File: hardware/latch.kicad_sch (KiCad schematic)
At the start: 4 parts, among them K2 2-1393779-0 TE, Q4 BSS123

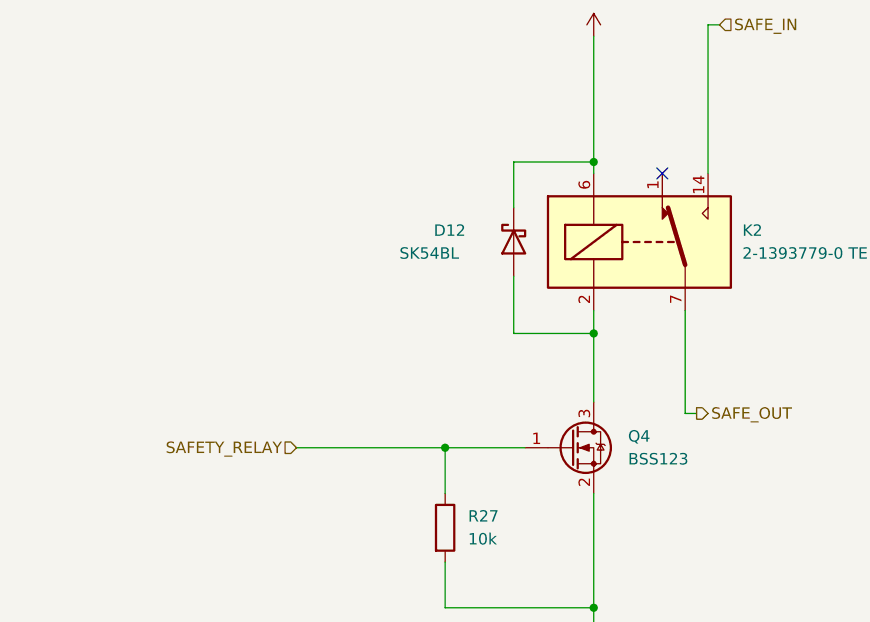
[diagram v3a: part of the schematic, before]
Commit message: 0xERC State
Schematic needs only simulation and veryfying component choice for now
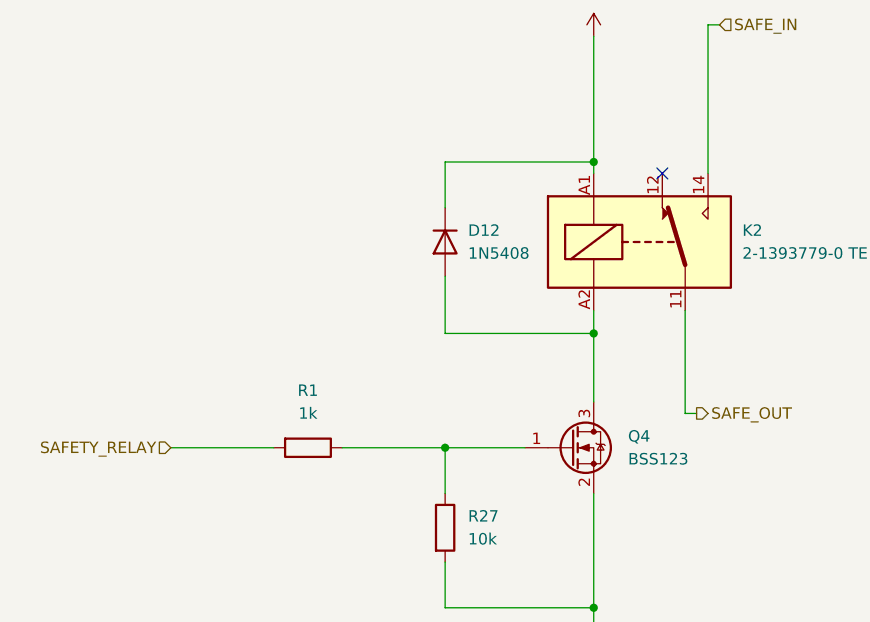
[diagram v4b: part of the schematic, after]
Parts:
- removed D12: SK54BL, Diode_SMD:D_SMB, symbol Device:D_Schottky
- added D12: 1N5408, Diode_THT:D_DO-201AD_P15.24mm_Horizontal, symbol Diode:1N5408
- added R1: 1k, Resistor_SMD:R_0603_1608Metric, symbol Device:R
- K2: footprint Relay_THT:Relay_StandexMeder_DIP_LowProfile -> PUTM_Kicad_FOOTPRINTS:TE Relay; symbol Relay:DIPxx-1Cxx-51x -> PUTM_SYMBOLS:EBS_safety_realy
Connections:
- net +24V: now also K2.A1, D12.1 (K); no longer K2.6
- net SAFETY_RELAY: now also R1.2; no longer Q4.1 (G), R27.1
- net SAFE_OUT: now also K2.11; no longer K2.7, K2.8
- net at Q4.3 (D): now also K2.A2, D12.2 (A); no longer K2.2
- new net: Q4.1 (G), R1.1, R27.1
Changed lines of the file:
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@@
     (company "PUT Motorsport")
   )
+  (junction (at 127 107.95) (diameter 0) (color 0 0 0 0)
+  )
   (junction (at 143.51 125.73) (diameter 0) (color 0 0 0 0)
-  )
-  (junction (at 127 107.95) (diameter 0) (color 0 0 0 0)
   )
   (junction (at 143.51 76.2) (diameter 0) (color 0 0 0 0)
@@
   )
   (no_connect (at 151.13 77.47))
-  (wire (pts (xy 110.49 107.95) (xy 127 107.95))
-    (stroke (width 0) (type default) (color 0 0 0 0))
-  )
-  (wire (pts (xy 134.62 88.9) (xy 134.62 95.25))
-    (stroke (width 0) (type default) (color 0 0 0 0))
-  )
   (wire (pts (xy 143.51 125.73) (xy 143.51 134.62))
     (stroke (width 0) (type default) (color 0 0 0 0))
@@
     (stroke (width 0) (type default) (color 0 0 0 0))
   )
-  (wire (pts (xy 134.62 95.25) (xy 143.51 95.25))
+  (wire (pts (xy 127 95.25) (xy 143.51 95.25))
     (stroke (width 0) (type default) (color 0 0 0 0))
   )
@@
     (stroke (width 0) (type default) (color 0 0 0 0))
   )
-  (wire (pts (xy 134.62 81.28) (xy 134.62 76.2))
+  (wire (pts (xy 127 81.28) (xy 127 76.2))
+    (stroke (width 0) (type default) (color 0 0 0 0))
+  )
+  (wire (pts (xy 127 76.2) (xy 143.51 76.2))
+    (stroke (width 0) (type default) (color 0 0 0 0))
+  )
+  (wire (pts (xy 96.52 107.95) (xy 107.95 107.95))
+    (stroke (width 0) (type default) (color 0 0 0 0))
+  )
+  (wire (pts (xy 115.57 107.95) (xy 127 107.95))
     (stroke (width 0) (type default) (color 0 0 0 0))
   )
@@
     (stroke (width 0) (type default) (color 0 0 0 0))
   )
-  (wire (pts (xy 134.62 76.2) (xy 143.51 76.2))
-    (stroke (width 0) (type default) (color 0 0 0 0))
-  )
   (wire (pts (xy 156.21 60.96) (xy 157.48 60.96))
     (stroke (width 0) (type default) (color 0 0 0 0))
   )
   (wire (pts (xy 143.51 113.03) (xy 143.51 125.73))
+    (stroke (width 0) (type default) (color 0 0 0 0))
+  )
+  (wire (pts (xy 127 95.25) (xy 127 88.9))
     (stroke (width 0) (type default) (color 0 0 0 0))
   )
@@
     (effects (font (size 1.27 1.27)) (justify left))
   )
-  (hierarchical_label "SAFETY_RELAY" (shape input) (at 110.49 107.95 180)
+  (hierarchical_label "SAFETY_RELAY" (shape input) (at 96.52 107.95 180)
     (effects (font (size 1.27 1.27)) (justify right))
   )
-  (symbol (lib_id "Relay:DIPxx-1Cxx-51x") (at 148.59 85.09 0) (unit 1)
+  (symbol (lib_id "Diode:1N5408") (at 127 85.09 90) (mirror x) (unit 1)
+    (in_bom yes) (on_board yes) (fields_autoplaced)
+    (property "Reference" "D12" (id 0) (at 129.54 83.8199 90)
+      (effects (font (size 1.27 1.27)) (justify right))
+    )
+    (property "Value" "1N5408" (id 1) (at 129.54 86.3599 90)
+      (effects (font (size 1.27 1.27)) (justify right))
+    )
+    (property "Footprint" "Diode_THT:D_DO-201AD_P15.24mm_Horizontal" (id 2) (at 131.445 85.09 0)
+      (effects (font (size 1.27 1.27)) hide)
+    )
+    (property "Datasheet" "http://www.vishay.com/docs/88516/1n5400.pdf" (id 3) (at 127 85.09 0)
+      (effects (font (size 1.27 1.27)) hide)
+    )
+    (pin "1")
+    (pin "2")
+  )
+  (symbol (lib_id "PUTM_SYMBOLS:EBS_safety_realy") (at 148.59 85.09 0) (unit 1)
     (in_bom yes) (on_board yes) (fields_autoplaced)
     (property "Reference" "K2" (id 0) (at 160.02 83.8199 0)
@@
       (effects (font (size 1.27 1.27)) (justify left))
     )
-    (property "Footprint" "Relay_THT:Relay_StandexMeder_DIP_LowProfile" (id 2) (at 160.02 86.36 0)
-      (effects (font (size 1.27 1.27)) (justify left) hide)
-    )
-    (property "Datasheet" "https://standexelectronics.com/wp-content/uploads/datasheet_reed_relay_DIP.pdf" (id 3) (at 148.59 85.09 0)
+    (property "Footprint" "PUTM_Kicad_FOOTPRINTS:TE Relay" (id 2) (at 148.59 76.2 0)
       (effects (font (size 1.27 1.27)) hide)
     )
-    (pin "1")
+    (property "Datasheet" "https://standexelectronics.com/wp-content/uploads/datasheet_reed_relay_DIP.pdf" (id 3) (at 148.59 76.2 0)
+      (effects (font (size 1.27 1.27)) hide)
+    )
+    (pin "11")
+    (pin "12")
     (pin "14")
-    (pin "2")
-    (pin "6")
-    (pin "7")
-    (pin "8")
+    (pin "A1")
+    (pin "A2")
   )
   (symbol (lib_id "power:GND") (at 143.51 134.62 0) (unit 1)
@@
     (pin "3")
   )
-  (symbol (lib_id "Device:D_Schottky") (at 134.62 85.09 90) (mirror x) (unit 1)
-    (in_bom yes) (on_board yes)
-    (property "Reference" "D12" (id 0) (at 125.73 83.82 90)
-      (effects (font (size 1.27 1.27)) (justify right))
-    )
-    (property "Value" "SK54BL" (id 1) (at 121.92 86.36 90)
-      (effects (font (size 1.27 1.27)) (justify right))
-    )
-    (property "Footprint" "Diode_SMD:D_SMB" (id 2) (at 134.62 85.09 0)
-      (effects (font (size 1.27 1.27)) hide)
-    )
-    (property "Datasheet" "~" (id 3) (at 134.62 85.09 0)
-      (effects (font (size 1.27 1.27)) hide)
-    )
-    (pin "1")
-    (pin "2")
-  )
   (symbol (lib_id "power:+24V") (at 143.51 62.23 0) (unit 1)
     (in_bom yes) (on_board yes) (fields_autoplaced)
@@
       (effects (font (size 1.27 1.27)) hide)
     )
+    (pin "1")
+    (pin "2")
+  )
+  (symbol (lib_id "Device:R") (at 111.76 107.95 270) (unit 1)
+    (in_bom yes) (on_board yes) (fields_autoplaced)
+    (property "Reference" "R1" (id 0) (at 111.76 101.6 90))
+    (property "Value" "1k" (id 1) (at 111.76 104.14 90))
+    (property "Footprint" "Resistor_SMD:R_0603_1608Metric" (id 2) (at 111.76 106.172 90)
+      (effects (font (size 1.27 1.27)) hide)
+    )
+    (property "Datasheet" "~" (id 3) (at 111.76 107.95 0)
+      (effects (font (size 1.27 1.27)) hide)
+    )

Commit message: working simulations, assigned footprints
"nightly" relase
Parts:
- removed K2: 2-1393779-0 TE, PUTM_Kicad_FOOTPRINTS:TE Relay, symbol PUTM_SYMBOLS:EBS_safety_realy
- added K2: FINDER-30.22, Relay_THT:Relay_DPDT_Finder_30.22, symbol Relay:FINDER-30.22
- D12: value 1N5408 -> SK36A; footprint Diode_THT:D_DO-201AD_P15.24mm_Horizontal -> Diode_SMD:D_SMA_Handsoldering
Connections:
- net +24V: now also K2.A1
- net SAFE_IN: now also K2.14
- net SAFE_OUT: now also K2.11
- net at D12.2 (A), Q4.3 (D): now also K2.A2
- no-connect marks 1 -> 4
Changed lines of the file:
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@@
   (junction (at 143.51 95.25) (diameter 0) (color 0 0 0 0)
   )
+  (no_connect (at 163.83 92.71))
+  (no_connect (at 161.29 77.47))
+  (no_connect (at 166.37 77.47))
   (no_connect (at 151.13 77.47))
   (wire (pts (xy 143.51 125.73) (xy 143.51 134.62))
@@
       (effects (font (size 1.27 1.27)) (justify right))
     )
-    (property "Value" "1N5408" (id 1) (at 129.54 86.3599 90)
+    (property "Value" "SK36A" (id 1) (at 129.54 86.3599 90)
       (effects (font (size 1.27 1.27)) (justify right))
     )
-    (property "Footprint" "Diode_THT:D_DO-201AD_P15.24mm_Horizontal" (id 2) (at 131.445 85.09 0)
+    (property "Footprint" "Diode_SMD:D_SMA_Handsoldering" (id 2) (at 131.445 85.09 0)
       (effects (font (size 1.27 1.27)) hide)
     )
-    (property "Datasheet" "http://www.vishay.com/docs/88516/1n5400.pdf" (id 3) (at 127 85.09 0)
+    (property "Datasheet" "https://www.mouser.pl/datasheet/2/395/SK32A_SERIES_V2102-2822194.pdf" (id 3) (at 127 85.09 0)
       (effects (font (size 1.27 1.27)) hide)
     )
     (pin "1")
     (pin "2")
-  )
-  (symbol (lib_id "PUTM_SYMBOLS:EBS_safety_realy") (at 148.59 85.09 0) (unit 1)
-    (in_bom yes) (on_board yes) (fields_autoplaced)
-    (property "Reference" "K2" (id 0) (at 160.02 83.8199 0)
-      (effects (font (size 1.27 1.27)) (justify left))
-    )
-    (property "Value" "2-1393779-0 TE" (id 1) (at 160.02 86.3599 0)
-      (effects (font (size 1.27 1.27)) (justify left))
-    )
-    (property "Footprint" "PUTM_Kicad_FOOTPRINTS:TE Relay" (id 2) (at 148.59 76.2 0)
-      (effects (font (size 1.27 1.27)) hide)
-    )
-    (property "Datasheet" "https://standexelectronics.com/wp-content/uploads/datasheet_reed_relay_DIP.pdf" (id 3) (at 148.59 76.2 0)
-      (effects (font (size 1.27 1.27)) hide)
-    )
-    (pin "11")
-    (pin "12")
-    (pin "14")
-    (pin "A1")
-    (pin "A2")
   )
   (symbol (lib_id "power:GND") (at 143.51 134.62 0) (unit 1)
@@
     (pin "2")
   )
+  (symbol (lib_id "Relay:FINDER-30.22") (at 153.67 85.09 0) (unit 1)
+    (in_bom yes) (on_board yes) (fields_autoplaced)
+    (property "Reference" "K2" (id 0) (at 170.18 81.28 0)
+      (effects (font (size 1.27 1.27)) (justify left))
+    )
+    (property "Value" "FINDER-30.22" (id 1) (at 170.18 83.82 0)
+      (effects (font (size 1.27 1.27)) (justify left))
+    )
+    (property "Footprint" "Relay_THT:Relay_DPDT_Finder_30.22" (id 2) (at 187.96 85.852 0)
+      (effects (font (size 1.27 1.27)) hide)
+    )
+    (property "Datasheet" "http://gfinder.findernet.com/assets/Series/354/S30EN.pdf" (id 3) (at 153.67 85.09 0)
+      (effects (font (size 1.27 1.27)) hide)
+    )
+    (pin "11")
+    (pin "12")
+    (pin "14")
+    (pin "21")
+    (pin "22")
+    (pin "24")
+    (pin "A1")
+    (pin "A2")
+  )
 )

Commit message: kończymy balet na dziś
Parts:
- R1, R27: footprint Resistor_SMD:R_0603_1608Metric -> Resistor_SMD:R_0603_1608Metric_Pad0.98x0.95mm_HandSolder
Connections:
- net VALVE_SUPPLY: now reaches K2.21
- net LINE: now reaches K2.24
- no-connect marks 4 -> 2
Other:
- note added: "LINE means supply connected After LVMS-> ASMS-> RES-> 2 Required by T15 2.2"
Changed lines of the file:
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@@
   (junction (at 143.51 125.73) (diameter 0) (color 0 0 0 0)
   )
+  (junction (at 166.37 48.26) (diameter 0) (color 0 0 0 0)
+  )
   (junction (at 143.51 76.2) (diameter 0) (color 0 0 0 0)
   )
   (junction (at 143.51 95.25) (diameter 0) (color 0 0 0 0)
   )
-  (no_connect (at 163.83 92.71))
   (no_connect (at 161.29 77.47))
-  (no_connect (at 166.37 77.47))
   (no_connect (at 151.13 77.47))
   (wire (pts (xy 143.51 125.73) (xy 143.51 134.62))
@@
     (stroke (width 0) (type default) (color 0 0 0 0))
   )
+  (wire (pts (xy 156.21 48.26) (xy 156.21 45.72))
+    (stroke (width 0) (type default) (color 0 0 0 0))
+  )
   (wire (pts (xy 127 95.25) (xy 143.51 95.25))
     (stroke (width 0) (type default) (color 0 0 0 0))
@@
     (stroke (width 0) (type default) (color 0 0 0 0))
   )
+  (wire (pts (xy 166.37 48.26) (xy 156.21 48.26))
+    (stroke (width 0) (type default) (color 0 0 0 0))
+  )
   (wire (pts (xy 127 81.28) (xy 127 76.2))
     (stroke (width 0) (type default) (color 0 0 0 0))
@@
     (stroke (width 0) (type default) (color 0 0 0 0))
   )
+  (wire (pts (xy 166.37 48.26) (xy 166.37 77.47))
+    (stroke (width 0) (type default) (color 0 0 0 0))
+  )
+  (wire (pts (xy 163.83 97.79) (xy 163.83 92.71))
+    (stroke (width 0) (type default) (color 0 0 0 0))
+  )
   (wire (pts (xy 96.52 107.95) (xy 107.95 107.95))
     (stroke (width 0) (type default) (color 0 0 0 0))
   )
+  (wire (pts (xy 201.93 97.79) (xy 163.83 97.79))
+    (stroke (width 0) (type default) (color 0 0 0 0))
+  )
   (wire (pts (xy 115.57 107.95) (xy 127 107.95))
     (stroke (width 0) (type default) (color 0 0 0 0))
@@
     (stroke (width 0) (type default) (color 0 0 0 0))
   )
-  (wire (pts (xy 156.21 60.96) (xy 156.21 77.47))
+  (wire (pts (xy 156.21 59.69) (xy 156.21 77.47))
     (stroke (width 0) (type default) (color 0 0 0 0))
   )
@@
     (stroke (width 0) (type default) (color 0 0 0 0))
   )
-  (wire (pts (xy 156.21 60.96) (xy 157.48 60.96))
-    (stroke (width 0) (type default) (color 0 0 0 0))
-  )
   (wire (pts (xy 143.51 113.03) (xy 143.51 125.73))
     (stroke (width 0) (type default) (color 0 0 0 0))
@@
     (stroke (width 0) (type default) (color 0 0 0 0))
   )
-  (hierarchical_label "SAFE_IN" (shape input) (at 157.48 60.96 0)
+  (wire (pts (xy 166.37 46.99) (xy 166.37 48.26))
+    (stroke (width 0) (type default) (color 0 0 0 0))
+  )
+  (text "LINE means supply connected After LVMS-> ASMS-> RES-> 2\nRequired by T15 2.2"
+    (at 171.45 58.42 0)
+    (effects (font (size 1.27 1.27) italic) (justify left bottom))
+  )
+  (hierarchical_label "VALVE_SUPPLY" (shape output) (at 201.93 97.79 0)
+    (effects (font (size 1.27 1.27)) (justify left))
+  )
+  (hierarchical_label "SAFE_IN" (shape input) (at 156.21 59.69 90)
     (effects (font (size 1.27 1.27)) (justify left))
   )
@@
     (pin "2")
   )
+  (symbol (lib_id "power:PWR_FLAG") (at 156.21 45.72 0) (unit 1)
+    (in_bom yes) (on_board yes) (fields_autoplaced)
+    (property "Reference" "#FLG0101" (id 0) (at 156.21 43.815 0)
+      (effects (font (size 1.27 1.27)) hide)
+    )
+    (property "Value" "PWR_FLAG" (id 1) (at 156.21 40.64 0))
+    (property "Footprint" "" (id 2) (at 156.21 45.72 0)
+      (effects (font (size 1.27 1.27)) hide)
+    )
+    (property "Datasheet" "~" (id 3) (at 156.21 45.72 0)
+      (effects (font (size 1.27 1.27)) hide)
+    )
+    (pin "1")
+  )
   (symbol (lib_id "power:GND") (at 143.51 134.62 0) (unit 1)
     (in_bom yes) (on_board yes) (fields_autoplaced)
@@
     (pin "1")
   )
+  (symbol (lib_id "power:LINE") (at 166.37 46.99 0) (unit 1)
+    (in_bom yes) (on_board yes) (fields_autoplaced)
+    (property "Reference" "#PWR0107" (id 0) (at 166.37 50.8 0)
+      (effects (font (size 1.27 1.27)) hide)
+    )
+    (property "Value" "LINE" (id 1) (at 166.37 41.91 0))
+    (property "Footprint" "" (id 2) (at 166.37 46.99 0)
+      (effects (font (size 1.27 1.27)) hide)
+    )
+    (property "Datasheet" "" (id 3) (at 166.37 46.99 0)
+      (effects (font (size 1.27 1.27)) hide)
+    )
+    (pin "1")
+  )
   (symbol (lib_id "Device:R") (at 127 116.84 0) (unit 1)
     (in_bom yes) (on_board yes) (fields_autoplaced)
@@
       (effects (font (size 1.27 1.27)) (justify left))
     )
-    (property "Footprint" "Resistor_SMD:R_0603_1608Metric" (id 2) (at 125.222 116.84 90)
+    (property "Footprint" "Resistor_SMD:R_0603_1608Metric_Pad0.98x0.95mm_HandSolder" (id 2) (at 125.222 116.84 90)
       (effects (font (size 1.27 1.27)) hide)
     )
@@
     (property "Reference" "R1" (id 0) (at 111.76 101.6 90))
     (property "Value" "1k" (id 1) (at 111.76 104.14 90))
-    (property "Footprint" "Resistor_SMD:R_0603_1608Metric" (id 2) (at 111.76 106.172 90)
-      (effects (font (size 1.27 1.27)) hide)
-    )
+    (property "Footprint" "Resistor_SMD:R_0603_1608Metric_Pad0.98x0.95mm_HandSolder" (id 2) (at 111.76 106.172 90)
+      (effects (font (size 1.27 1.27)) hide)
+    )
